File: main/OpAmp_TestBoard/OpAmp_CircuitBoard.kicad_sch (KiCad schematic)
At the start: 13 parts, among them U1 LM358

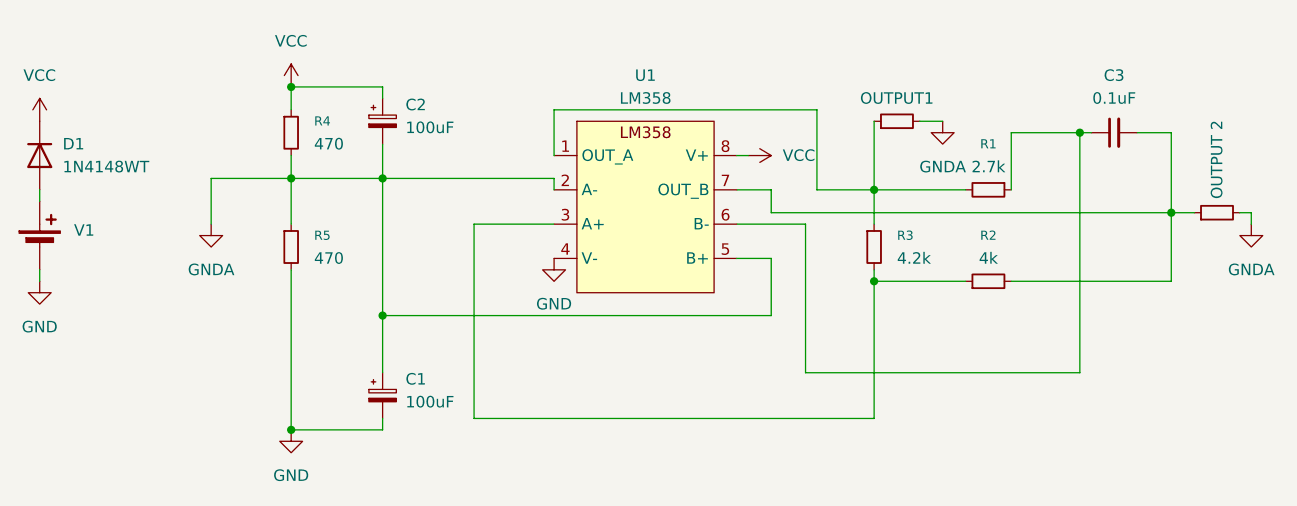
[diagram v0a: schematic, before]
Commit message: Created new documents folder for Common Emitter Circuit
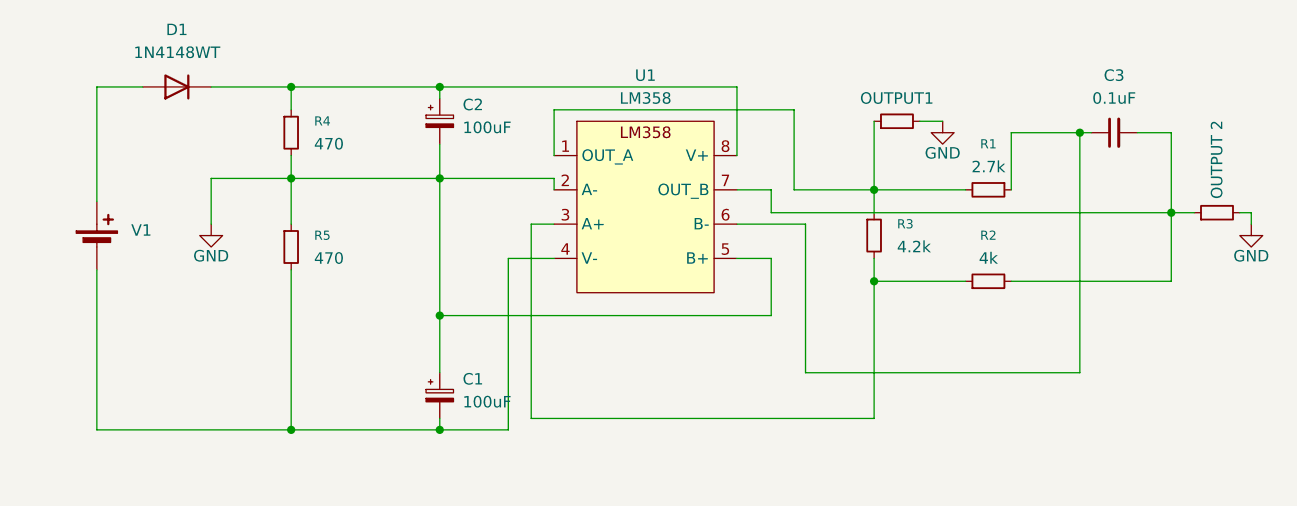
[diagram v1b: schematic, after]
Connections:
- net GNDA is gone; now on net GND: C1.1, C2.2, R4.2, R5.1, R6.2, R7.2, U1.2 (A-), U1.5 (B+)
- net GND: no longer C1.2, R5.2, U1.4 (V-), V1.2 (-)
- net VCC: no longer names the net of C2.1, D1.1 (K), R4.1, U1.8 (V+)
- new net: C1.2, R5.2, U1.4 (V-), V1.2 (-)
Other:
- moved on the sheet: C1, C2, D1, R3, V1
